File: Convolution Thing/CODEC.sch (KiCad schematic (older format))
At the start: 14 parts

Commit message: Convolution Thing PCB design continues
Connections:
- net labels added: ADC1LN, ADC1LP, ADC1RN, ADC1RP, ADC2LN, ADC2LP, ADC2RN, ADC2RP, ADCDATA1, ADCDATA2, DAC1LN, DAC1LP, DAC1RN, DAC1RP, DAC2LN, DAC2LP, DAC2RN, DAC2RP, DAC3LN, DAC3LP, DAC3RN, DAC3RP, DAC4LN, DAC4LP, DAC4RN, DAC4RP, DACDATA1, DACDATA2, DACDATA3, DACDATA4
- net labels removed: DNGD
- wire segments 37 -> 67
- no-connect marks 0 -> 11
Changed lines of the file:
@@
 $Descr A4 11693 8268
 encoding utf-8
-Sheet 2 4
+Sheet 2 7
 Title ""
 Date ""
@@
 Wire Wire Line
 	5800 3250 5500 3250
-Text Label 1900 1650 2    50   ~ 0
-AGND
-Text Label 1900 1950 2    50   ~ 0
-AGND
-Text Label 4000 3150 0    50   ~ 0
-DNGD
-Text Label 4000 1850 0    50   ~ 0
-AGND
-Text Label 4000 2050 0    50   ~ 0
-AGND
-Text Label 4000 1750 0    50   ~ 0
+Text Label 1650 2000 2    50   ~ 0
+AGND
+Text Label 1650 2300 2    50   ~ 0
+AGND
+Text Label 3750 3500 0    50   ~ 0
+DGND
+Text Label 3750 2200 0    50   ~ 0
+AGND
+Text Label 3750 2400 0    50   ~ 0
+AGND
+Text Label 3750 2100 0    50   ~ 0
 FILTR
 Text Label 5500 1000 0    50   ~ 0
@@
 Wire Wire Line
 	6950 2250 7400 2250
-Text Label 4000 1950 0    50   ~ 0
+Text Label 3750 2300 0    50   ~ 0
 AVDD
-Text Label 1900 2050 2    50   ~ 0
+Text Label 1650 2400 2    50   ~ 0
 AVDD
 Text Label 6900 1000 0    50   ~ 0
@@
 Wire Wire Line
 	5500 1000 5500 1300
-Text Label 4000 1650 0    50   ~ 0
-AGND
-Text Label 4000 2950 0    50   ~ 0
+Text Label 3750 2000 0    50   ~ 0
+AGND
+Text Label 3750 3300 0    50   ~ 0
 DGND
 Text Label 5850 1000 0    50   ~ 0
@@
 Wire Wire Line
 	5850 1000 5850 1300
-Text Label 3500 3950 3    50   ~ 0
+Text Label 3250 4300 3    50   ~ 0
 DGND
-Text GLabel 3400 4400 3    50   Output ~ 0
+Text GLabel 3150 4550 3    50   Output ~ 0
 LRCLK
 Wire Wire Line
 	6250 3250 6400 3250
 Connection ~ 6250 3250
-Wire Wire Line
-	3400 4400 3400 3950
-Text GLabel 3300 4150 3    50   Output ~ 0
+Text GLabel 3050 4550 3    50   Output ~ 0
 BCLK
-Wire Wire Line
-	3300 4150 3300 3950
-Text Label 1900 3150 2    50   ~ 0
+Text Label 1650 3500 2    50   ~ 0
 DGND
-Text Label 2500 950  1    50   ~ 0
+Text Label 2250 1300 1    50   ~ 0
 LF
 Text Label 9350 1950 2    50   ~ 0
@@
 Text Label 9350 2850 2    50   ~ 0
 AVDD
-Text Label 2400 950  1    50   ~ 0
+Text Label 2150 1300 1    50   ~ 0
 AVDD
-Text Label 3500 950  1    50   ~ 0
+Text Label 3250 1300 1    50   ~ 0
 AVDD
 $Comp
@@
 	9950 2850 9950 2550
 Connection ~ 9450 2850
-Text Label 3400 950  1    50   ~ 0
+Text Label 3150 1300 1    50   ~ 0
 CM
 Text Label 8100 1950 2    50   ~ 0
@@
 Wire Wire Line
 	6100 2000 5900 2000
-Text Label 1900 2950 2    50   ~ 0
+Text Label 1650 3300 2    50   ~ 0
 RST
 $Comp
@@
 L SamacSys:AD1937WBSTZ IC?
 U 1 1 61052169
-P 1900 1650
-F 0 "IC?" H 2900 900 50  0000 L CNN
-F 1 "AD1937WBSTZ" H 2700 800 50  0000 L CNN
-F 2 "QFP50P1200X1200X160-64N" H 3850 2150 50  0001 L CNN
-F 3 "https://componentsearchengine.com/Datasheets/2/AD1937WBSTZ.pdf" H 3850 2050 50  0001 L CNN
-F 4 "Analog Devices, Audio Codec Stereo Audio 12-channel 24bit- 192kHz Serial 64-Pin LQFP" H 3850 1950 50  0001 L CNN "Description"
-F 5 "1.6" H 3850 1850 50  0001 L CNN "Height"
-F 6 "584-AD1937WBSTZ" H 3850 1750 50  0001 L CNN "Mouser Part Number"
-F 7 "https://www.mouser.co.uk/ProductDetail/Analog-Devices/AD1937WBSTZ?qs=NmRFExCfTkGjgJ1ByCN4rw%3D%3D" H 3850 1650 50  0001 L CNN "Mouser Price/Stock"
-F 8 "Analog Devices" H 3850 1550 50  0001 L CNN "Manufacturer_Name"
-F 9 "AD1937WBSTZ" H 3850 1450 50  0001 L CNN "Manufacturer_Part_Number"
-	1    1900 1650
-	1    0    0    -1
-$EndComp
-Text Label 2200 3950 3    50   ~ 0
+P 1650 2000
+F 0 "IC?" H 2650 1250 50  0000 L CNN
+F 1 "AD1937WBSTZ" H 2450 1150 50  0000 L CNN
+F 2 "QFP50P1200X1200X160-64N" H 3600 2500 50  0001 L CNN
+F 3 "https://componentsearchengine.com/Datasheets/2/AD1937WBSTZ.pdf" H 3600 2400 50  0001 L CNN
+F 4 "Analog Devices, Audio Codec Stereo Audio 12-channel 24bit- 192kHz Serial 64-Pin LQFP" H 3600 2300 50  0001 L CNN "Description"
+F 5 "1.6" H 3600 2200 50  0001 L CNN "Height"
+F 6 "584-AD1937WBSTZ" H 3600 2100 50  0001 L CNN "Mouser Part Number"
+F 7 "https://www.mouser.co.uk/ProductDetail/Analog-Devices/AD1937WBSTZ?qs=NmRFExCfTkGjgJ1ByCN4rw%3D%3D" H 3600 2000 50  0001 L CNN "Mouser Price/Stock"
+F 8 "Analog Devices" H 3600 1900 50  0001 L CNN "Manufacturer_Name"
+F 9 "AD1937WBSTZ" H 3600 1800 50  0001 L CNN "Manufacturer_Part_Number"
+	1    1650 2000
+	1    0    0    -1
+$EndComp
+Text Label 1950 4300 3    50   ~ 0
 DVDD
-Text Label 3700 3950 3    50   ~ 0
+Text Label 3450 4300 3    50   ~ 0
 DVDD
 Text Label 5500 3250 2    50   ~ 0
@@
 Wire Wire Line
 	6250 2800 6250 2850
-Text Label 3600 3950 3    50   ~ 0
+Text Label 3350 4300 3    50   ~ 0
 SDA
 Text Label 5500 3750 2    50   ~ 0
@@
 	6400 3750 5800 3750
 Connection ~ 5800 3750
-Text Label 4000 3050 0    50   ~ 0
+Text Label 3750 3400 0    50   ~ 0
 SCL
+Text GLabel 4000 3200 2    50   Output ~ 0
+DAC1LP
+Text GLabel 4000 3100 2    50   Output ~ 0
+DAC1LN
+Text GLabel 4000 3000 2    50   Output ~ 0
+DAC1RP
+Text GLabel 4000 2800 2    50   Output ~ 0
+DAC2LP
+Text GLabel 4000 2600 2    50   Output ~ 0
+DAC2RP
+Text GLabel 4000 2900 2    50   Output ~ 0
+DAC1RN
+Text GLabel 4000 2700 2    50   Output ~ 0
+DAC2LN
+Text GLabel 4000 2500 2    50   Output ~ 0
+DAC2RN
+Wire Wire Line
+	4000 3200 3750 3200
+Wire Wire Line
+	4000 3000 3750 3000
+Wire Wire Line
+	4000 2800 3750 2800
+Wire Wire Line
+	4000 2600 3750 2600
+Text GLabel 1400 2500 0    50   Output ~ 0
+DAC3LP
+Text GLabel 1400 2700 0    50   Output ~ 0
+DAC3RP
+Text GLabel 1400 2900 0    50   Output ~ 0
+DAC4LP
+Text GLabel 1400 3100 0    50   Output ~ 0
+DAC4RP
+Text GLabel 1400 3200 0    50   Output ~ 0
+DAC4RN
+Text GLabel 1400 3000 0    50   Output ~ 0
+DAC4LN
+Text GLabel 1400 2800 0    50   Output ~ 0
+DAC3RN
+Text GLabel 1400 2600 0    50   Output ~ 0
+DAC3LN
+Wire Wire Line
+	1400 2500 1650 2500
+Wire Wire Line
+	1650 2700 1400 2700
+Wire Wire Line
+	1400 2900 1650 2900
+Wire Wire Line
+	1650 3100 1400 3100
+Text GLabel 2350 1150 1    50   Input ~ 0
+ADC2RN
+Text GLabel 2550 1150 1    50   Input ~ 0
+ADC2LN
+Text GLabel 2750 1150 1    50   Input ~ 0
+ADC1RN
+Text GLabel 2950 1150 1    50   Input ~ 0
+ADC1LN
+Text GLabel 3050 1150 1    50   Input ~ 0
+ADC1LP
+Text GLabel 2850 1150 1    50   Input ~ 0
+ADC1RP
+Text GLabel 2650 1150 1    50   Input ~ 0
+ADC2LP
+Text GLabel 2450 1150 1    50   Input ~ 0
+ADC2RP
+Wire Wire Line
+	1400 3200 1650 3200
+Wire Wire Line
+	1650 3000 1400 3000
+Wire Wire Line
+	1400 2800 1650 2800
+Wire Wire Line
+	1650 2600 1400 2600
+Wire Wire Line
+	3750 3100 4000 3100
+Wire Wire Line
+	4000 2900 3750 2900
+Wire Wire Line
+	3750 2700 4000 2700
+Wire Wire Line
+	4000 2500 3750 2500
+Wire Wire Line
+	2350 1300 2350 1150
+Wire Wire Line
+	2450 1150 2450 1300
+Wire Wire Line
+	2550 1300 2550 1150
+Wire Wire Line
+	2650 1150 2650 1300
+Wire Wire Line
+	2750 1300 2750 1150
+Wire Wire Line
+	2850 1150 2850 1300
+Wire Wire Line
+	2950 1300 2950 1150
+Wire Wire Line
+	3050 1150 3050 1300
+Text GLabel 2950 4550 3    50   Output ~ 0
+ADCDATA1
+Wire Wire Line
+	3050 4300 3050 4550
+Wire Wire Line
+	3150 4550 3150 4300
+Text GLabel 2850 4550 3    50   Output ~ 0
+ADCDATA2
+Wire Wire Line
+	2850 4550 2850 4300
+Wire Wire Line
+	2950 4300 2950 4550
+Text GLabel 2250 4550 3    50   Input ~ 0
+DACDATA1
+Text GLabel 2150 4550 3    50   Input ~ 0
+DACDATA2
+Text GLabel 2050 4550 3    50   Input ~ 0
+DACDATA3
+Text GLabel 1400 3400 0    50   Input ~ 0
+DACDATA4
+Wire Wire Line
+	1400 3400 1650 3400
+Wire Wire Line
+	2250 4550 2250 4300
+Wire Wire Line
+	2150 4300 2150 4550
+Wire Wire Line
+	2050 4550 2050 4300
+NoConn ~ 2050 1300
+NoConn ~ 1950 1300
+NoConn ~ 3350 1300
+NoConn ~ 3450 1300
+NoConn ~ 1650 2100
+NoConn ~ 1650 2200
+NoConn ~ 2750 4300
+NoConn ~ 2650 4300
+NoConn ~ 2550 4300
+NoConn ~ 2450 4300
+NoConn ~ 2350 4300
 $EndSCHEMATC

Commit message: Work on CODEC and In/Out stages
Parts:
- added C? (x4): 100nF, symbol Device:C
- C? (x2): value 10uF -> 100nF
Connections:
- net labels added: AVDD1, AVDD2, AVDD3, AVDD4, DVDD1, DVDD2
- net labels removed: DVDD
- wire segments 67 -> 80
- no-connect marks 11 -> 8
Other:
- moved on the sheet: C?, R?

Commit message: New stereo codec and related changes. RIP multi-channel audio.
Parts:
- removed C?: 10uF, symbol Device:C
- removed C? (x8): 100nF, symbol Device:C
- removed C?: 5.6nF, symbol Device:CP1
- removed C?: 390pF, symbol Device:C
- removed C?: 47uF, symbol Device:C
- removed IC?: AD1937WBSTZ, QFP50P1200X1200X160-64N, symbol SamacSys:AD1937WBSTZ
- removed R?: 10k, symbol Device:R
- removed R?: 2k, symbol Device:R
- removed R?: 562, symbol Device:R
- removed TP?: SCL TP, symbol Connector:TestPoint
- removed TP?: SDA TP, symbol Connector:TestPoint
- added C? (x3): 10uF, symbol Device:CP1
- added C? (x3): 100nF, symbol Device:C
- added IC?: PCM3060PW, SOP65P640X120-28N, symbol SamacSys:PCM3060PW
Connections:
- net labels added: +5VA, ADC_OUT, ADC_VIN_L, ADC_VIN_R, ADR, BCK, CODEC_VCOM, DAC_IN, DAC_VOUT_L+, DAC_VOUT_L-, DAC_VOUT_R+, DAC_VOUT_R-, LRCK, MODE, SGND, VCC, VCOM, VDD
- net labels removed: +3.3VA, ADC1LN, ADC1LP, ADC1RN, ADC1RP, ADC2LN, ADC2LP, ADC2RN, ADC2RP, ADCDATA1, ADCDATA2, AVDD, AVDD1, AVDD2, AVDD3, AVDD4, BCLK, CM, DAC1LN, DAC1LP, DAC1RN, DAC1RP, DAC2LN, DAC2LP, DAC2RN, DAC2RP, DAC3LN, DAC3LP, DAC3RN, DAC3RP, DAC4LN, DAC4LP, DAC4RN, DAC4RP, DACDATA1, DACDATA2, DACDATA3, DACDATA4, DVDD1, DVDD2, FILTR, LF, LRCLK, RST
- wire segments 80 -> 29
- no-connect marks 8 -> 7
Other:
- note added: "I2C Address = 0"
- note added: "I2C Mode"

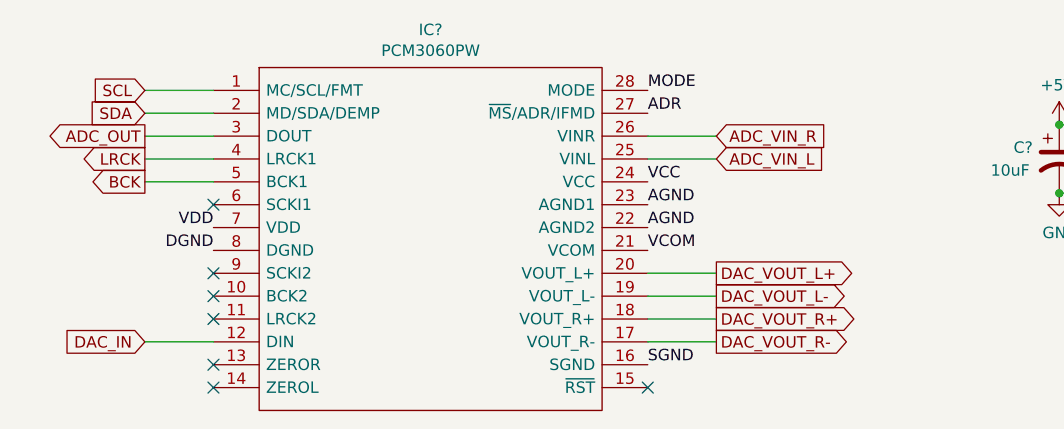
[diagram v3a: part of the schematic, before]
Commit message: Audio I/O, CV input, GPIO work & misc changes
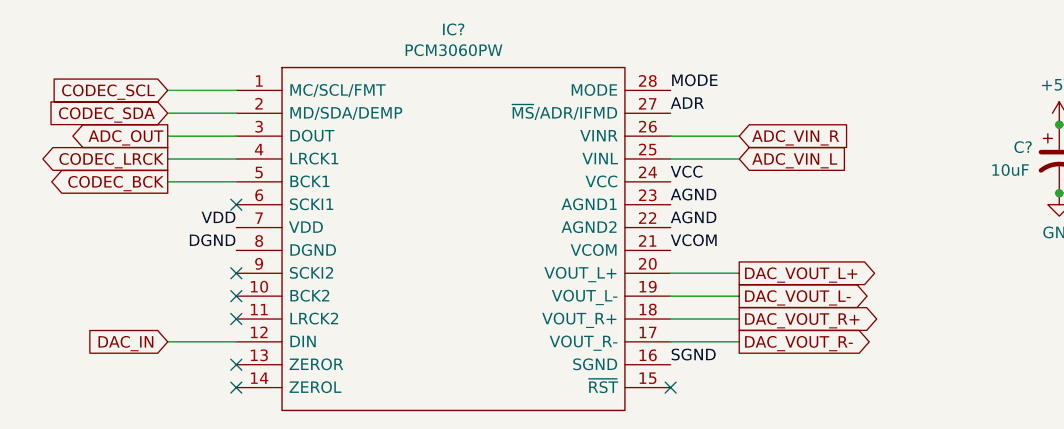
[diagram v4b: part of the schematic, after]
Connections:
- net BCK renamed CODEC_BCK
- net LRCK renamed CODEC_LRCK
- net SCL renamed CODEC_SCL
- net SDA renamed CODEC_SDA
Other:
- moved on the sheet: IC?
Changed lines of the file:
@@
 $Descr A4 11693 8268
 encoding utf-8
-Sheet 2 7
+Sheet 2 9
 Title ""
 Date ""
@@
 Comment4 ""
 $EndDescr
-Text Label 1300 1450 2    50   ~ 0
+Text Label 1400 1450 2    50   ~ 0
 VDD
 Text Label 5500 1000 0    50   ~ 0
@@
 	5250 1300 5000 1300
 Connection ~ 5000 1300
-Text Label 1300 1550 2    50   ~ 0
+Text Label 1400 1550 2    50   ~ 0
 DGND
-Text Label 3200 1350 0    50   ~ 0
+Text Label 3300 1350 0    50   ~ 0
 AGND
-Text Label 3200 1450 0    50   ~ 0
+Text Label 3300 1450 0    50   ~ 0
 AGND
-Text Label 3200 2050 0    50   ~ 0
+Text Label 3300 2050 0    50   ~ 0
 SGND
 Text Label 8500 1000 0    50   ~ 0
@@
 Wire Wire Line
 	8500 1150 8500 1000
-Text Label 3200 1250 0    50   ~ 0
+Text Label 3300 1250 0    50   ~ 0
 VCC
 Text Label 6550 1000 0    50   ~ 0
@@
 $EndComp
 Connection ~ 5000 1000
-Text Label 3200 1550 0    50   ~ 0
+Text Label 3300 1550 0    50   ~ 0
 VCOM
 Text Label 7100 1000 2    50   ~ 0
@@
 	7750 1000 7350 1000
 Connection ~ 7350 1000
-Text Label 3200 850  0    50   ~ 0
+Text Label 3300 850  0    50   ~ 0
 MODE
 Text Label 9600 1000 2    50   ~ 0
@@
 L SamacSys:PCM3060PW IC?
 U 1 1 610925E3
-P 1300 850
-F 0 "IC?" H 2250 1115 50  0000 C CNN
-F 1 "PCM3060PW" H 2250 1024 50  0000 C CNN
-F 2 "SOP65P640X120-28N" H 3050 950 50  0001 L CNN
-F 3 "http://componentsearchengine.com/Datasheets/1/PCM3060PW.pdf" H 3050 850 50  0001 L CNN
-F 4 "24-bit Asynchronous Stereo Audio Codec with 96/192kHz sampling rate" H 3050 750 50  0001 L CNN "Description"
-F 5 "1.2" H 3050 650 50  0001 L CNN "Height"
-F 6 "595-PCM3060PW" H 3050 550 50  0001 L CNN "Mouser Part Number"
-F 7 "https://www.mouser.co.uk/ProductDetail/Texas-Instruments/PCM3060PW?qs=W5eanQMd1BDLVsOltr0iFA%3D%3D" H 3050 450 50  0001 L CNN "Mouser Price/Stock"
-F 8 "Texas Instruments" H 3050 350 50  0001 L CNN "Manufacturer_Name"
-F 9 "PCM3060PW" H 3050 250 50  0001 L CNN "Manufacturer_Part_Number"
-	1    1300 850
-	1    0    0    -1
-$EndComp
-NoConn ~ 3200 2150
-NoConn ~ 1300 2050
-NoConn ~ 1300 2150
-NoConn ~ 1300 1650
-NoConn ~ 1300 1350
-NoConn ~ 1300 1750
-NoConn ~ 1300 1850
-Text GLabel 1000 1150 0    50   Output ~ 0
-LRCK
-Text GLabel 1000 1250 0    50   Output ~ 0
-BCK
-Text GLabel 1000 850  0    50   Input ~ 0
-SCL
-Text GLabel 1000 950  0    50   Input ~ 0
-SDA
-Text GLabel 1000 1050 0    50   Output ~ 0
+P 1400 850
+F 0 "IC?" H 2350 1115 50  0000 C CNN
+F 1 "PCM3060PW" H 2350 1024 50  0000 C CNN
+F 2 "SOP65P640X120-28N" H 3150 950 50  0001 L CNN
+F 3 "http://componentsearchengine.com/Datasheets/1/PCM3060PW.pdf" H 3150 850 50  0001 L CNN
+F 4 "24-bit Asynchronous Stereo Audio Codec with 96/192kHz sampling rate" H 3150 750 50  0001 L CNN "Description"
+F 5 "1.2" H 3150 650 50  0001 L CNN "Height"
+F 6 "595-PCM3060PW" H 3150 550 50  0001 L CNN "Mouser Part Number"
+F 7 "https://www.mouser.co.uk/ProductDetail/Texas-Instruments/PCM3060PW?qs=W5eanQMd1BDLVsOltr0iFA%3D%3D" H 3150 450 50  0001 L CNN "Mouser Price/Stock"
+F 8 "Texas Instruments" H 3150 350 50  0001 L CNN "Manufacturer_Name"
+F 9 "PCM3060PW" H 3150 250 50  0001 L CNN "Manufacturer_Part_Number"
+	1    1400 850
+	1    0    0    -1
+$EndComp
+NoConn ~ 3300 2150
+NoConn ~ 1400 2050
+NoConn ~ 1400 2150
+NoConn ~ 1400 1650
+NoConn ~ 1400 1350
+NoConn ~ 1400 1750
+NoConn ~ 1400 1850
+Text GLabel 1100 1150 0    50   Output ~ 0
+CODEC_LRCK
+Text GLabel 1100 1250 0    50   Output ~ 0
+CODEC_BCK
+Text GLabel 1100 850  0    50   Input ~ 0
+CODEC_SCL
+Text GLabel 1100 950  0    50   Input ~ 0
+CODEC_SDA
+Text GLabel 1100 1050 0    50   Output ~ 0
 ADC_OUT
-Text GLabel 1000 1950 0    50   Input ~ 0
+Text GLabel 1100 1950 0    50   Input ~ 0
 DAC_IN
-Text Label 3200 950  0    50   ~ 0
+Text Label 3300 950  0    50   ~ 0
 ADR
 Text Label 10200 1000 2    50   ~ 0
@@
 Text Notes 9950 1600 0    50   ~ 0
 I2C Address = 0
-Text GLabel 3500 1050 2    50   Input ~ 0
+Text GLabel 3600 1050 2    50   Input ~ 0
 ADC_VIN_R
-Text GLabel 3500 1150 2    50   Input ~ 0
+Text GLabel 3600 1150 2    50   Input ~ 0
 ADC_VIN_L
-Text GLabel 3500 1650 2    50   Output ~ 0
+Text GLabel 3600 1650 2    50   Output ~ 0
 DAC_VOUT_L+
-Text GLabel 3500 1750 2    50   Output ~ 0
+Text GLabel 3600 1750 2    50   Output ~ 0
 DAC_VOUT_L-
-Text GLabel 3500 1850 2    50   Output ~ 0
+Text GLabel 3600 1850 2    50   Output ~ 0
 DAC_VOUT_R+
-Text GLabel 3500 1950 2    50   Output ~ 0
+Text GLabel 3600 1950 2    50   Output ~ 0
 DAC_VOUT_R-
 Wire Wire Line
-	3500 1950 3200 1950
-Wire Wire Line
-	3200 1850 3500 1850
-Wire Wire Line
-	3500 1750 3200 1750
-Wire Wire Line
-	3200 1650 3500 1650
-Wire Wire Line
-	3500 1150 3200 1150
-Wire Wire Line
-	3200 1050 3500 1050
-Wire Wire Line
-	1000 850  1300 850
-Wire Wire Line
-	1300 950  1000 950
-Wire Wire Line
-	1000 1050 1300 1050
-Wire Wire Line
-	1300 1150 1000 1150
-Wire Wire Line
-	1000 1250 1300 1250
-Wire Wire Line
-	1300 1950 1000 1950
+	3600 1950 3300 1950
+Wire Wire Line
+	3300 1850 3600 1850
+Wire Wire Line
+	3600 1750 3300 1750
+Wire Wire Line
+	3300 1650 3600 1650
+Wire Wire Line
+	3600 1150 3300 1150
+Wire Wire Line
+	3300 1050 3600 1050
+Wire Wire Line
+	1100 850  1400 850
+Wire Wire Line
+	1400 950  1100 950
+Wire Wire Line
+	1100 1050 1400 1050
+Wire Wire Line
+	1400 1150 1100 1150
+Wire Wire Line
+	1100 1250 1400 1250
+Wire Wire Line
+	1400 1950 1100 1950
 $EndSCHEMATC

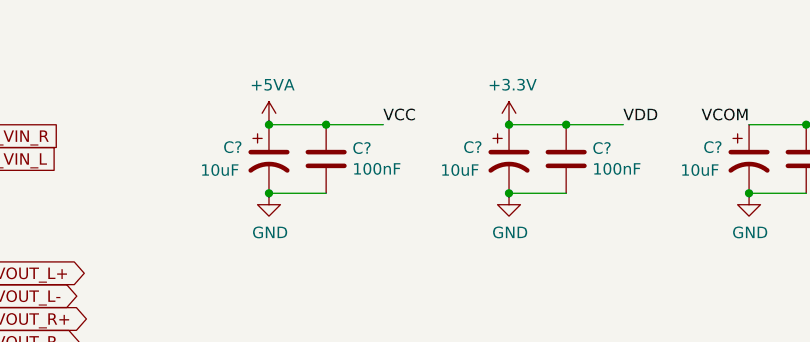
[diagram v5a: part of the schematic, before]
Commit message: Added gate inputs and CM4 / display sockets, made CV inputs 100k, lots of smaller changes. First iteration of schematic now done.
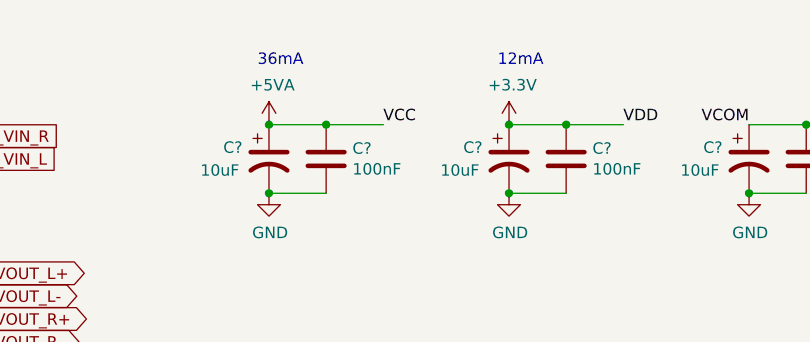
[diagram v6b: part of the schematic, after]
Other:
- note added: "12mA"
- note added: "36mA"
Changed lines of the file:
@@
 $Descr A4 11693 8268
 encoding utf-8
-Sheet 2 11
+Sheet 2 13
 Title ""
 Date ""
@@
 Wire Wire Line
 	1400 1950 1100 1950
+Text Notes 4950 750  0    50   ~ 0
+36mA
+Text Notes 6000 750  0    50   ~ 0
+12mA
 $EndSCHEMATC
